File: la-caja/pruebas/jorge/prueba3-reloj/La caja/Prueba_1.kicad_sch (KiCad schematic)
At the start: 2 parts

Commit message: Kicad - Cambios en el esquemático
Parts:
- gave numbers to parts that had none: 1
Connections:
- net at PRUEBA1.21 (D7(GPIO13)): now also KeyPad1.~ (8)
- net at PRUEBA1.22 (D6(GPIO12)): now also KeyPad1.~ (8)
- net at PRUEBA1.23 (D5(GPIO14)): now also KeyPad1.~ (8)
- net at PRUEBA1.26 (D4(GPIO2)): now also KeyPad1.~ (8)
- net at PRUEBA1.27 (D3(GPIO0)): now also KeyPad1.~ (8)
- net at PRUEBA1.28 (D2(GPIO4)): now also KeyPad1.~ (8)
- net at PRUEBA1.29 (D1(GPIO5)): now also KeyPad1.~ (8)
- net at PRUEBA1.30 (D0(GPIO16)): now also KeyPad1.~ (8)
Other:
- moved on the sheet: KeyPad1, PRUEBA1
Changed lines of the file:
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@@
     (company "Proyecto la Caja")
   )
-  (wire (pts (xy 147.32 86.36) (xy 162.56 86.36))
+  (wire (pts (xy 219.71 68.58) (xy 219.71 63.5))
     (stroke (width 0) (type default) (color 0 0 0 0))
   )
-  (wire (pts (xy 147.32 83.82) (xy 162.56 83.82))
+  (wire (pts (xy 177.8 55.88) (xy 222.25 55.88))
+    (stroke (width 0) (type default) (color 0 0 0 0))
+  )
+  (wire (pts (xy 177.8 53.34) (xy 222.25 53.34))
+    (stroke (width 0) (type default) (color 0 0 0 0))
+  )
+  (wire (pts (xy 177.8 50.8) (xy 222.25 50.8))
+    (stroke (width 0) (type default) (color 0 0 0 0))
+  )
+  (wire (pts (xy 177.8 60.96) (xy 222.25 60.96))
+    (stroke (width 0) (type default) (color 0 0 0 0))
+  )
+  (wire (pts (xy 220.98 71.12) (xy 220.98 66.04))
+    (stroke (width 0) (type default) (color 0 0 0 0))
+  )
+  (wire (pts (xy 177.8 73.66) (xy 222.25 73.66))
+    (stroke (width 0) (type default) (color 0 0 0 0))
+  )
+  (wire (pts (xy 147.32 86.36) (xy 137.16 86.36))
+    (stroke (width 0) (type default) (color 0 0 0 0))
+  )
+  (wire (pts (xy 220.98 66.04) (xy 222.25 66.04))
+    (stroke (width 0) (type default) (color 0 0 0 0))
+  )
+  (wire (pts (xy 219.71 63.5) (xy 222.25 63.5))
+    (stroke (width 0) (type default) (color 0 0 0 0))
+  )
+  (wire (pts (xy 222.25 73.66) (xy 222.25 68.58))
+    (stroke (width 0) (type default) (color 0 0 0 0))
+  )
+  (wire (pts (xy 177.8 58.42) (xy 222.25 58.42))
+    (stroke (width 0) (type default) (color 0 0 0 0))
+  )
+  (wire (pts (xy 177.8 68.58) (xy 219.71 68.58))
+    (stroke (width 0) (type default) (color 0 0 0 0))
+  )
+  (wire (pts (xy 177.8 71.12) (xy 220.98 71.12))
+    (stroke (width 0) (type default) (color 0 0 0 0))
+  )
+  (wire (pts (xy 147.32 83.82) (xy 137.16 83.82))
     (stroke (width 0) (type default) (color 0 0 0 0))
   )
@@
     (effects (font (size 1.27 1.27)) (justify right))
   )
-  (symbol (lib_id "ESP8266:NodeMCU1.0(ESP-12E)") (at 182.88 68.58 0) (unit 1)
+  (symbol (lib_id "ESP8266:NodeMCU1.0(ESP-12E)") (at 157.48 68.58 0) (unit 1)
     (in_bom yes) (on_board yes)
-    (property "Reference" "PRUEBA1" (id 0) (at 182.88 40.64 0)
+    (property "Reference" "PRUEBA1" (id 0) (at 157.48 40.64 0)
       (effects (font (size 1.524 1.524)))
     )
-    (property "Value" "NodeMCU1.0(ESP-12E)" (id 1) (at 182.88 44.45 0)
+    (property "Value" "NodeMCU1.0(ESP-12E)" (id 1) (at 157.48 44.45 0)
       (effects (font (size 1.524 1.524)))
     )
-    (property "Footprint" "" (id 2) (at 167.64 90.17 0)
+    (property "Footprint" "" (id 2) (at 142.24 90.17 0)
       (effects (font (size 1.524 1.524)))
     )
-    (property "Datasheet" "https://www.esploradores.com/wp-content/uploads/2019/11/PINOUT-NodeMCU_1.0-V2-2_2.jpg" (id 3) (at 182.88 93.98 0)
+    (property "Datasheet" "https://www.esploradores.com/wp-content/uploads/2019/11/PINOUT-NodeMCU_1.0-V2-2_2.jpg" (id 3) (at 157.48 93.98 0)
       (effects (font (size 1.524 1.524)))
     )
-    (property "Precio" "10€" (id 4) (at 182.88 68.58 0)
+    (property "Precio" "10€" (id 4) (at 157.48 68.58 0)
       (effects (font (size 1.27 1.27)) hide)
     )
@@
     (pin "9")
   )
-  (symbol (lib_id "KEYPAD:4x4_Keypad") (at 49.53 66.04 270) (unit 1)
+  (symbol (lib_id "KEYPAD:4x4_Keypad") (at 243.84 59.69 90) (mirror x) (unit 1)
     (in_bom yes) (on_board yes)
-    (property "Reference" "96BB2-006-F?" (id 0) (at 50.165 40.64 90)
+    (property "Reference" "KeyPad1" (id 0) (at 243.205 34.29 90)
       (effects (font (size 1.524 1.524)))
     )
-    (property "Value" "4x4_Keypad" (id 1) (at 50.165 44.45 90)
+    (property "Value" "4x4_Keypad" (id 1) (at 243.205 38.1 90)
       (effects (font (size 1.524 1.524)))
     )
-    (property "Footprint" "" (id 2) (at 49.53 66.04 0)
+    (property "Footprint" "" (id 2) (at 243.84 59.69 0)
       (effects (font (size 1.524 1.524)))
     )
-    (property "Datasheet" "" (id 3) (at 49.53 66.04 0)
+    (property "Datasheet" "" (id 3) (at 243.84 59.69 0)
       (effects (font (size 1.524 1.524)))
     )

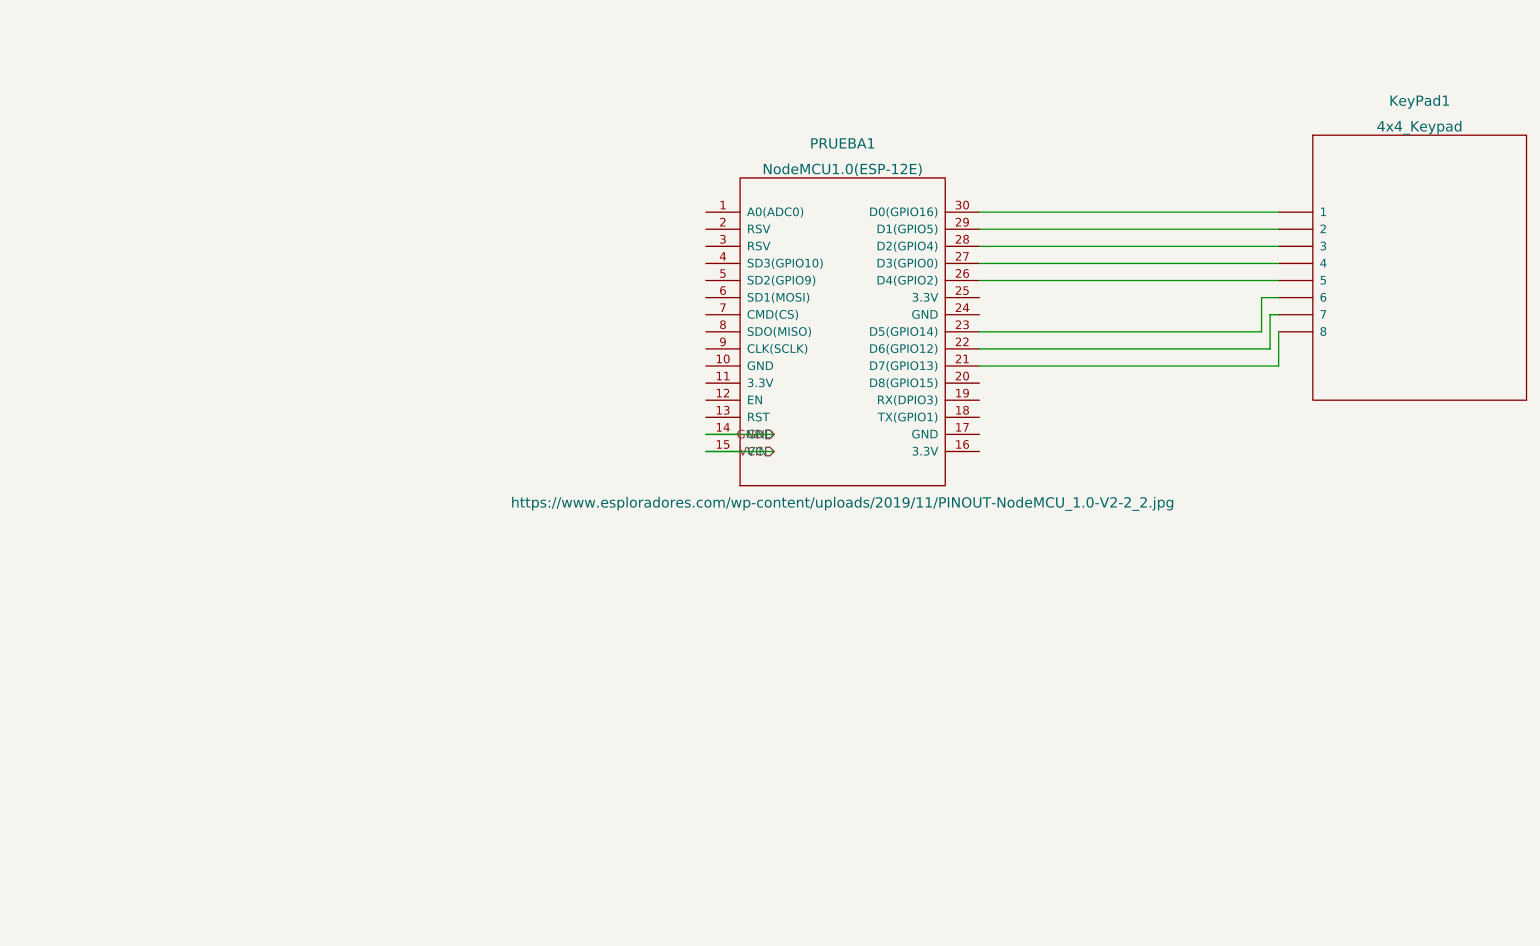
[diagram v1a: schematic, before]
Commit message: Cara002 demo funcional
Contiene:
- La clase infra y todas las necesarias para su correcto
funcionamiento
- Conexión con Node-Red y base de datos (local por ahora)
- Conexión con dashboard y timers (a decidir)
- Funciones extra para procesamiento de la información
- Mecánicas del juego con el formato de FSM.
- Envío constante del estado del juego
- Bugs detectados:
  - Las cifras que empiezan por cero no las detecta bien, por ejemplo
  si una delas soluciones es "0002", el programa se buguearía hasta
  que el usuario introduzca una cifra "correcta"
- Features:
  - Añadir pistas para el usuario:
    - Caliente o frío (facilita demasiado el juego, pista de nivel dificil)
    - Explicar el acertijo
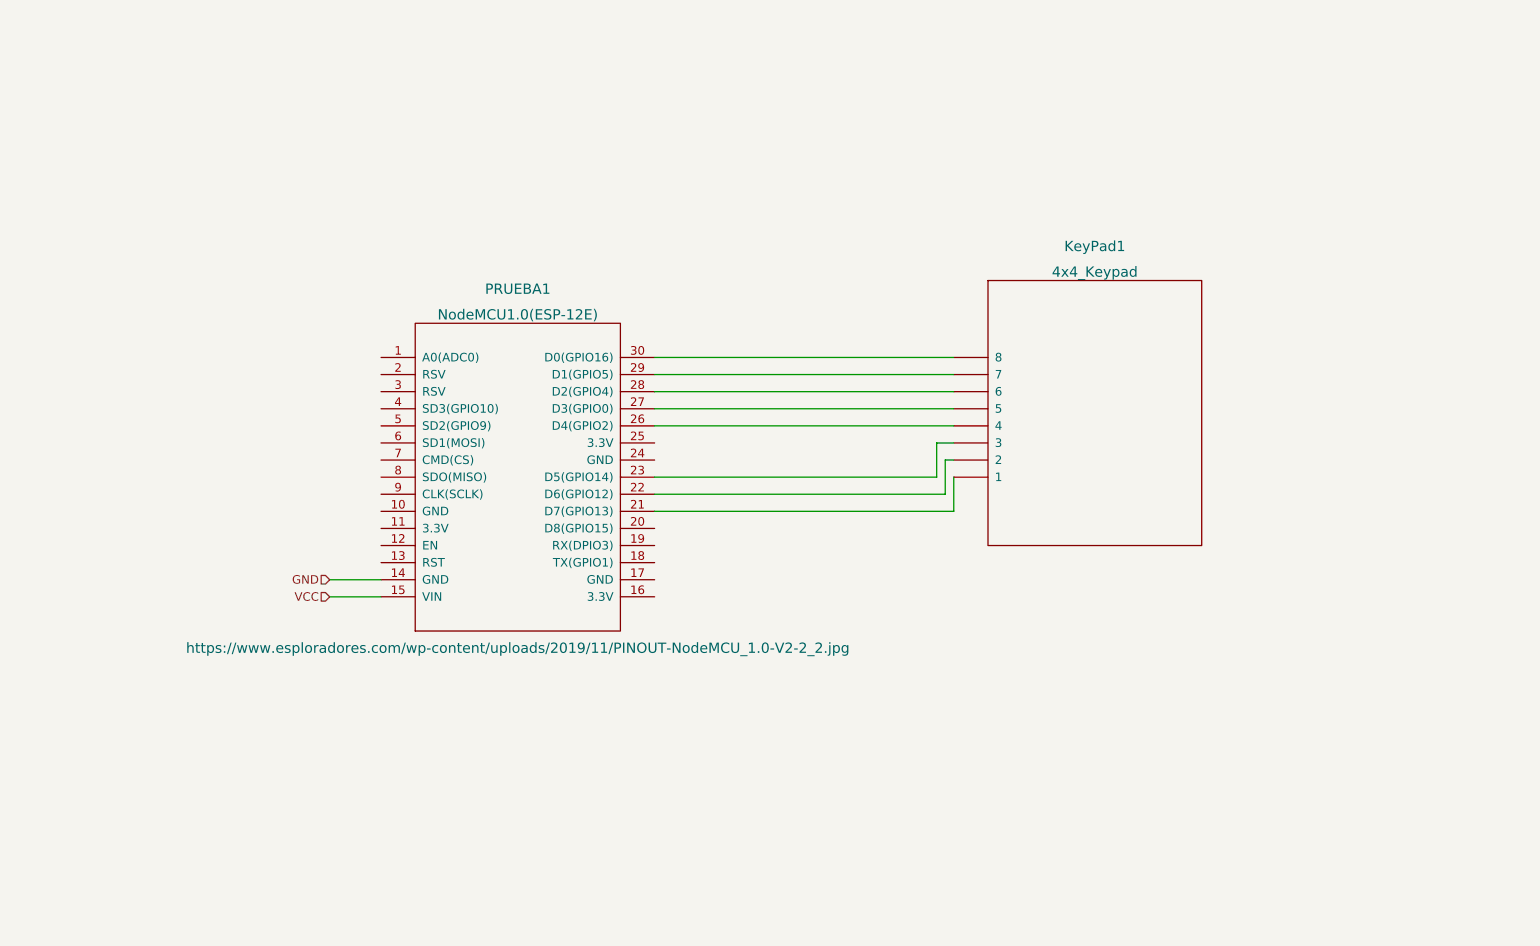
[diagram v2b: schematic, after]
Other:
- moved on the sheet: KeyPad1, PRUEBA1
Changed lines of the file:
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@@
     (company "Proyecto la Caja")
   )
-  (wire (pts (xy 219.71 68.58) (xy 219.71 63.5))
+  (wire (pts (xy 171.45 90.17) (xy 171.45 85.09))
     (stroke (width 0) (type default) (color 0 0 0 0))
   )
-  (wire (pts (xy 177.8 55.88) (xy 222.25 55.88))
+  (wire (pts (xy 129.54 77.47) (xy 173.99 77.47))
     (stroke (width 0) (type default) (color 0 0 0 0))
   )
-  (wire (pts (xy 177.8 53.34) (xy 222.25 53.34))
+  (wire (pts (xy 129.54 74.93) (xy 173.99 74.93))
     (stroke (width 0) (type default) (color 0 0 0 0))
   )
-  (wire (pts (xy 177.8 50.8) (xy 222.25 50.8))
+  (wire (pts (xy 129.54 72.39) (xy 173.99 72.39))
     (stroke (width 0) (type default) (color 0 0 0 0))
   )
-  (wire (pts (xy 177.8 60.96) (xy 222.25 60.96))
+  (wire (pts (xy 129.54 82.55) (xy 173.99 82.55))
     (stroke (width 0) (type default) (color 0 0 0 0))
   )
-  (wire (pts (xy 220.98 71.12) (xy 220.98 66.04))
+  (wire (pts (xy 172.72 92.71) (xy 172.72 87.63))
     (stroke (width 0) (type default) (color 0 0 0 0))
   )
-  (wire (pts (xy 177.8 73.66) (xy 222.25 73.66))
+  (wire (pts (xy 129.54 95.25) (xy 173.99 95.25))
     (stroke (width 0) (type default) (color 0 0 0 0))
   )
-  (wire (pts (xy 147.32 86.36) (xy 137.16 86.36))
+  (wire (pts (xy 81.28 107.95) (xy 88.9 107.95))
     (stroke (width 0) (type default) (color 0 0 0 0))
   )
-  (wire (pts (xy 220.98 66.04) (xy 222.25 66.04))
+  (wire (pts (xy 172.72 87.63) (xy 173.99 87.63))
     (stroke (width 0) (type default) (color 0 0 0 0))
   )
-  (wire (pts (xy 219.71 63.5) (xy 222.25 63.5))
+  (wire (pts (xy 171.45 85.09) (xy 173.99 85.09))
     (stroke (width 0) (type default) (color 0 0 0 0))
   )
-  (wire (pts (xy 222.25 73.66) (xy 222.25 68.58))
+  (wire (pts (xy 173.99 95.25) (xy 173.99 90.17))
     (stroke (width 0) (type default) (color 0 0 0 0))
   )
-  (wire (pts (xy 177.8 58.42) (xy 222.25 58.42))
+  (wire (pts (xy 129.54 80.01) (xy 173.99 80.01))
     (stroke (width 0) (type default) (color 0 0 0 0))
   )
-  (wire (pts (xy 177.8 68.58) (xy 219.71 68.58))
+  (wire (pts (xy 129.54 90.17) (xy 171.45 90.17))
     (stroke (width 0) (type default) (color 0 0 0 0))
   )
-  (wire (pts (xy 177.8 71.12) (xy 220.98 71.12))
+  (wire (pts (xy 129.54 92.71) (xy 172.72 92.71))
     (stroke (width 0) (type default) (color 0 0 0 0))
   )
-  (wire (pts (xy 147.32 83.82) (xy 137.16 83.82))
+  (wire (pts (xy 81.28 105.41) (xy 88.9 105.41))
     (stroke (width 0) (type default) (color 0 0 0 0))
   )
-  (hierarchical_label "GND" (shape input) (at 147.32 83.82 180)
+  (hierarchical_label "GND" (shape input) (at 81.28 105.41 180)
     (effects (font (size 1.27 1.27)) (justify right))
   )
-  (hierarchical_label "VCC" (shape input) (at 147.32 86.36 180)
+  (hierarchical_label "VCC" (shape input) (at 81.28 107.95 180)
     (effects (font (size 1.27 1.27)) (justify right))
   )
-  (symbol (lib_id "ESP8266:NodeMCU1.0(ESP-12E)") (at 157.48 68.58 0) (unit 1)
+  (symbol (lib_id "ESP8266:NodeMCU1.0(ESP-12E)") (at 109.22 90.17 0) (unit 1)
     (in_bom yes) (on_board yes)
-    (property "Reference" "PRUEBA1" (id 0) (at 157.48 40.64 0)
+    (property "Reference" "PRUEBA1" (id 0) (at 109.22 62.23 0)
       (effects (font (size 1.524 1.524)))
     )
-    (property "Value" "NodeMCU1.0(ESP-12E)" (id 1) (at 157.48 44.45 0)
+    (property "Value" "NodeMCU1.0(ESP-12E)" (id 1) (at 109.22 66.04 0)
       (effects (font (size 1.524 1.524)))
     )
-    (property "Footprint" "" (id 2) (at 142.24 90.17 0)
+    (property "Footprint" "" (id 2) (at 93.98 111.76 0)
       (effects (font (size 1.524 1.524)))
     )
-    (property "Datasheet" "https://www.esploradores.com/wp-content/uploads/2019/11/PINOUT-NodeMCU_1.0-V2-2_2.jpg" (id 3) (at 157.48 93.98 0)
+    (property "Datasheet" "https://www.esploradores.com/wp-content/uploads/2019/11/PINOUT-NodeMCU_1.0-V2-2_2.jpg" (id 3) (at 109.22 115.57 0)
       (effects (font (size 1.524 1.524)))
     )
-    (property "Precio" "10€" (id 4) (at 157.48 68.58 0)
+    (property "Precio" "10€" (id 4) (at 109.22 90.17 0)
       (effects (font (size 1.27 1.27)) hide)
     )
@@
     (pin "9")
   )
-  (symbol (lib_id "KEYPAD:4x4_Keypad") (at 243.84 59.69 90) (mirror x) (unit 1)
+  (symbol (lib_id "KEYPAD:4x4_Keypad") (at 195.58 81.28 90) (mirror x) (unit 1)
     (in_bom yes) (on_board yes)
-    (property "Reference" "KeyPad1" (id 0) (at 243.205 34.29 90)
+    (property "Reference" "KeyPad1" (id 0) (at 194.945 55.88 90)
       (effects (font (size 1.524 1.524)))
     )
-    (property "Value" "4x4_Keypad" (id 1) (at 243.205 38.1 90)
+    (property "Value" "4x4_Keypad" (id 1) (at 194.945 59.69 90)
       (effects (font (size 1.524 1.524)))
     )
-    (property "Footprint" "" (id 2) (at 243.84 59.69 0)
+    (property "Footprint" "" (id 2) (at 195.58 81.28 0)
       (effects (font (size 1.524 1.524)))
     )
-    (property "Datasheet" "" (id 3) (at 243.84 59.69 0)
+    (property "Datasheet" "" (id 3) (at 195.58 81.28 0)
       (effects (font (size 1.524 1.524)))
     )

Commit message: Cambios varios: Kicad, notas
- Símbolo del numpad hecho
- Notas sobre la primera prueba de la cara002
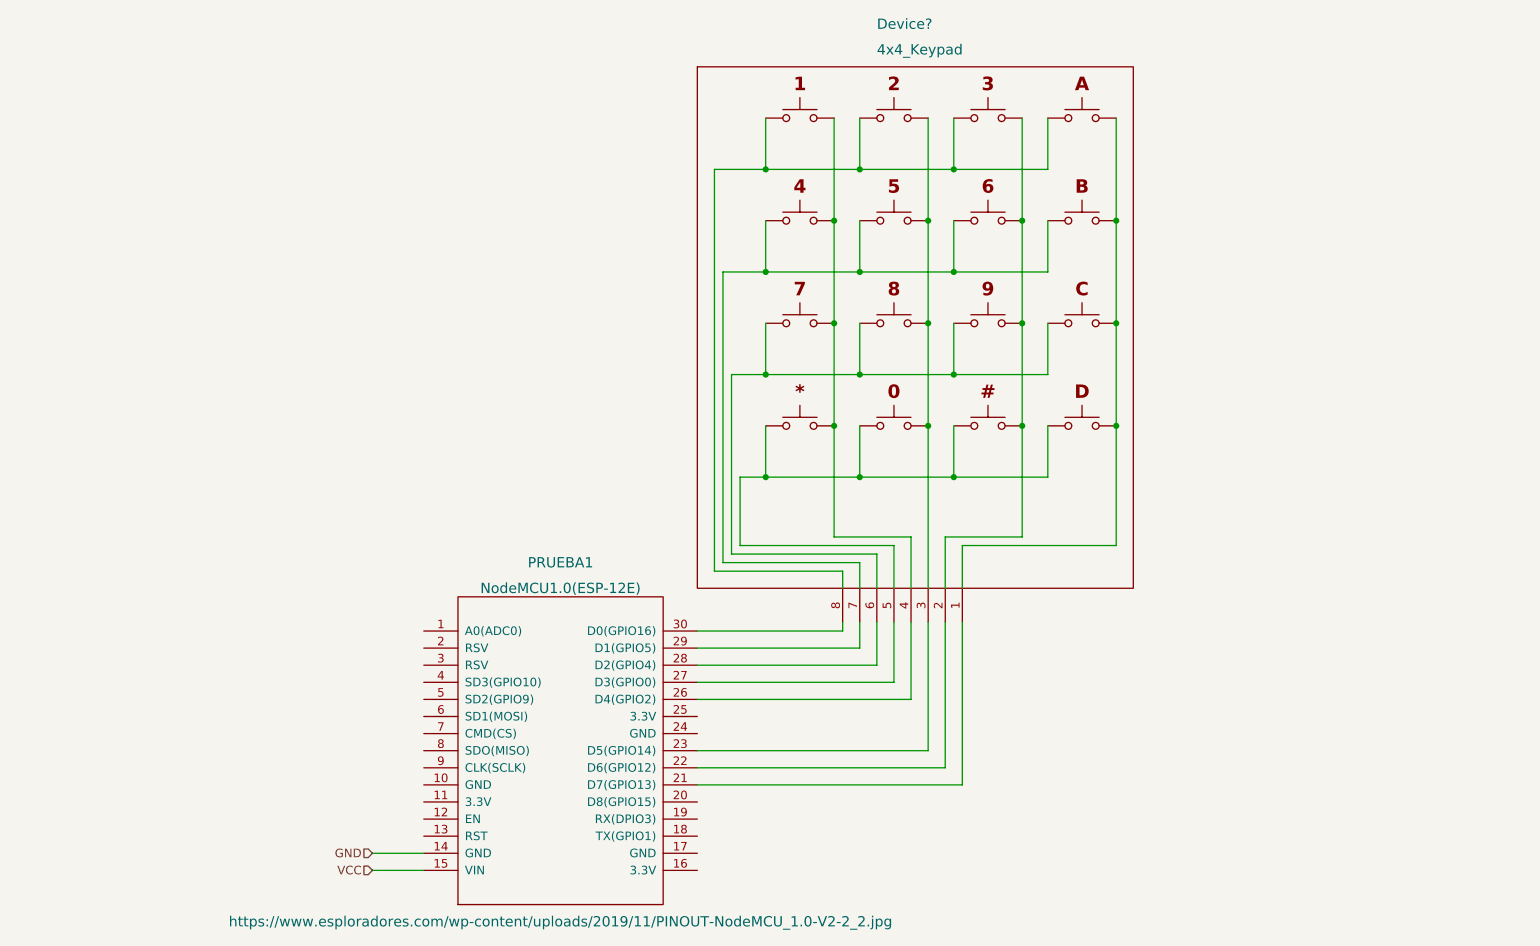
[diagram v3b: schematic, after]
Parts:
- removed KeyPad1: 4x4_Keypad, symbol KEYPAD:4x4_Keypad
- added Device?: 4x4_Keypad, symbol OwnKeyPAD:4x4_Keypad
- added SW? (x16): SW_Push, symbol Switch:SW_Push
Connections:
- net at PRUEBA1.21 (D7(GPIO13)): now also Device?.1
- net at PRUEBA1.22 (D6(GPIO12)): now also Device?.2
- net at PRUEBA1.23 (D5(GPIO14)): now also Device?.3
- net at PRUEBA1.26 (D4(GPIO2)): now also Device?.4
- net at PRUEBA1.27 (D3(GPIO0)): now also Device?.5
- net at PRUEBA1.28 (D2(GPIO4)): now also Device?.6
- net at PRUEBA1.29 (D1(GPIO5)): now also Device?.7
- net at PRUEBA1.30 (D0(GPIO16)): now also Device?.8
- new net: SW?.1, SW?.1, SW?.1, SW?.1 (x4)
- new net: SW?.2, SW?.2, SW?.2, SW?.2 (x4)
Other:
- moved on the sheet: PRUEBA1
